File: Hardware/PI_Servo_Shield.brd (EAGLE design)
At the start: 65 x 30 mm, 89 parts, among them J1 RASPBERRYPI-40-PIN-GPIO, J19 QWIIC, J20 USB C, J21 Serial, U1 PCA9685, U2 PCA9306, U3 CH340C

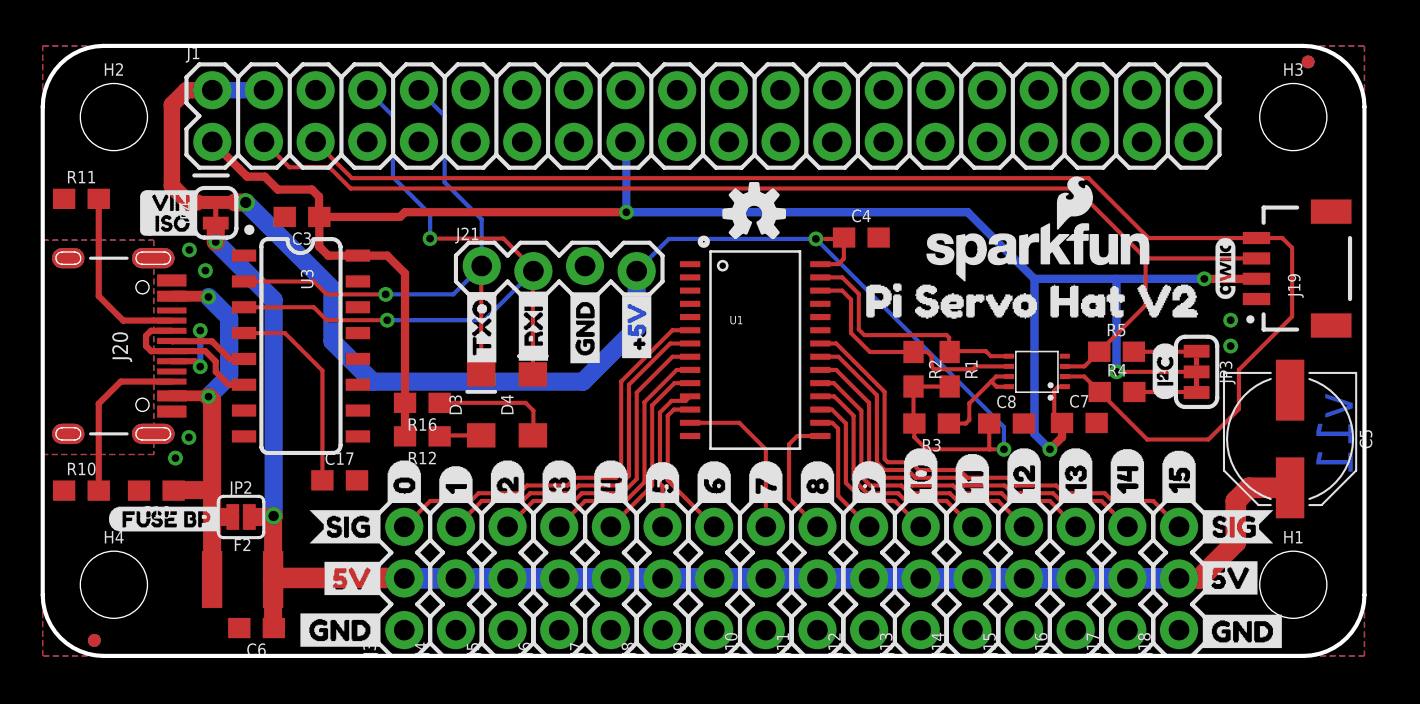
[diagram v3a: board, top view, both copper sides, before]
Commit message: post checklist changes - silk and testpoints
-silk outlines up to 8 mil on a few.
-testpoints
-RX/TX LED colors corrected
-some PROD_ID stuff fixed.
-text note in sch for i2c jumper
-voltage warning for > +5V RVR input damaging pi.
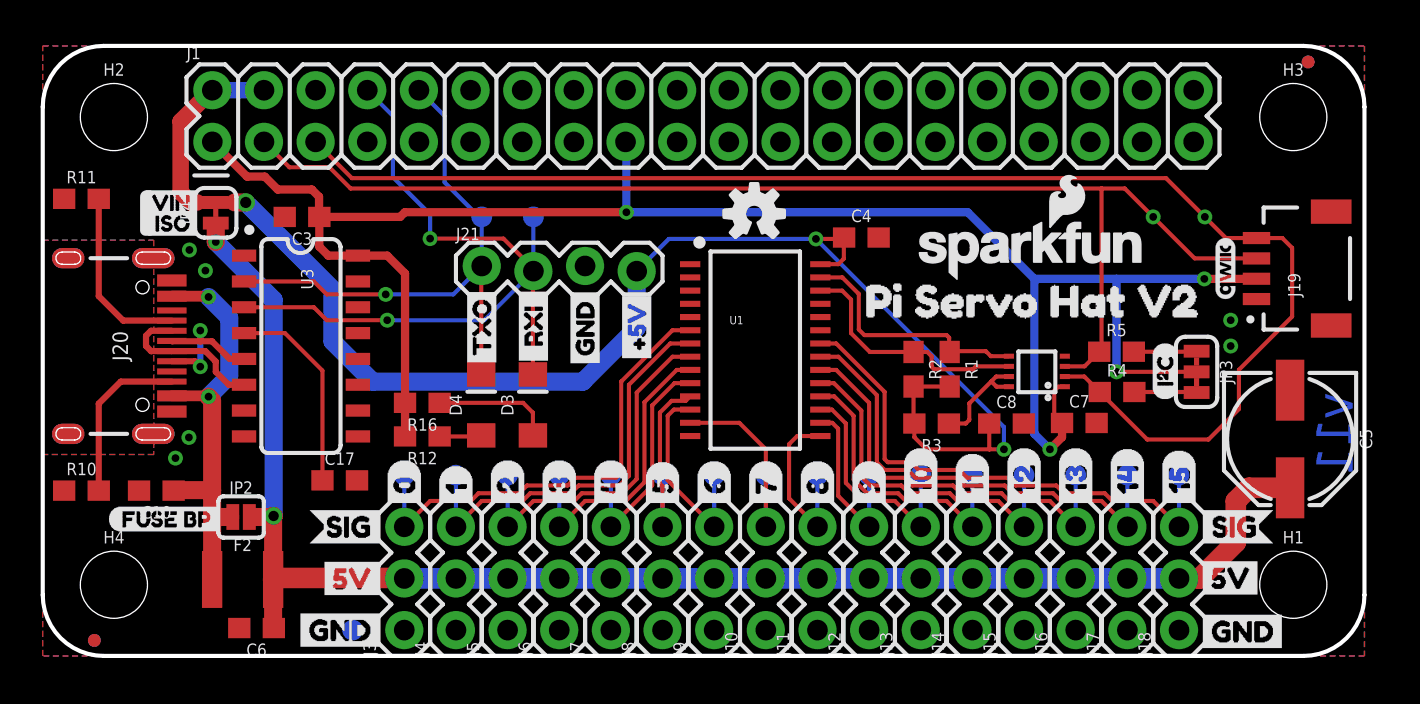
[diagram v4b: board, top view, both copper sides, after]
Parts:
- added TP0, TP1, TP10, TP11, TP12, TP13, TP14, TP15, TP16, TP17, TP2, TP20, TP21, TP3, TP4, TP5, TP6, TP7, TP8, TP9: (no value), SparkFun-Connectors:PAD.03X.04
- added TP18, TP19: (no value), SparkFun-Connectors:TP_15TH
- D4: device SparkFun-LED:LED-1206 -> SparkFun-LED:LED-1206-HIDDENSILK
- J20: device USB-C:USB-C-16P -> SparkFun-Connectors:USB-C-16P
- moved LOGO1 5.81 mm to (48.6, 20.0)
- moved D3 2.54 mm to (24.1, 12.3)
- moved D4 2.54 mm to (21.6, 12.3)
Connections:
- removed net N$12: D4.A, R16.1
- removed net N$13: D3.A, R12.1
- new net N$6: D3.A, R16.1
- new net N$7: D4.A, R12.1
- net CH0: now also TP0.P$1
- net CH1: now also TP1.P$1
- net CH10: now also TP10.P$1
- net CH11: now also TP11.P$1
- net CH12: now also TP12.P$1
- net CH13: now also TP13.P$1
- net CH14: now also TP14.P$1
- net CH15: now also TP15.P$1
- net CH2: now also TP2.P$1
- net CH3: now also TP3.P$1
- net CH4: now also TP4.P$1
- net CH5: now also TP5.P$1
- net CH6: now also TP6.P$1
- net CH7: now also TP7.P$1
- net CH8: now also TP8.P$1
- net CH9: now also TP9.P$1
- net GND: now also TP17.P$1
- net LV_SCL: now also TP18.P$1
- net LV_SDA: now also TP19.P$1
- net RXI: now also D3.C, TP20.P$1; no longer D4.C
- net TXO: now also D4.C, TP21.P$1; no longer D3.C
- net VIN: now also TP16.P$1
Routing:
- net N$12: track 6.00 -> 0.00 mm
- net N$6: track 0.00 -> 5.90 mm
- net RXI: track 35.1 -> 37.8 mm
- net VIN: track 75.5 -> 78.0 mm
- net CH14: track 20.5 -> 23.0 mm
- net CH12: track 14.8 -> 17.4 mm
- net CH0: track 20.7 -> 23.2 mm
- net CH9: track 6.45 -> 8.99 mm
- net CH8: track 6.35 -> 8.89 mm
- net CH5: track 7.49 -> 10.0 mm
- net CH7: track 8.07 -> 10.6 mm
- net CH6: track 7.64 -> 10.2 mm
- net CH4: track 9.13 -> 11.7 mm
- net CH3: track 11.9 -> 14.5 mm
- net CH11: track 12.0 -> 14.5 mm
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
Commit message: post double check stuff - moved from PCA9306 to transistors
-PCA level shifter is EOL, moved to transistor conversion.
-added VCC range note in SCH
-fixed a trace off of PCA PWM chip
-PROD_ID fixes on LEDs
-moved measure to show units
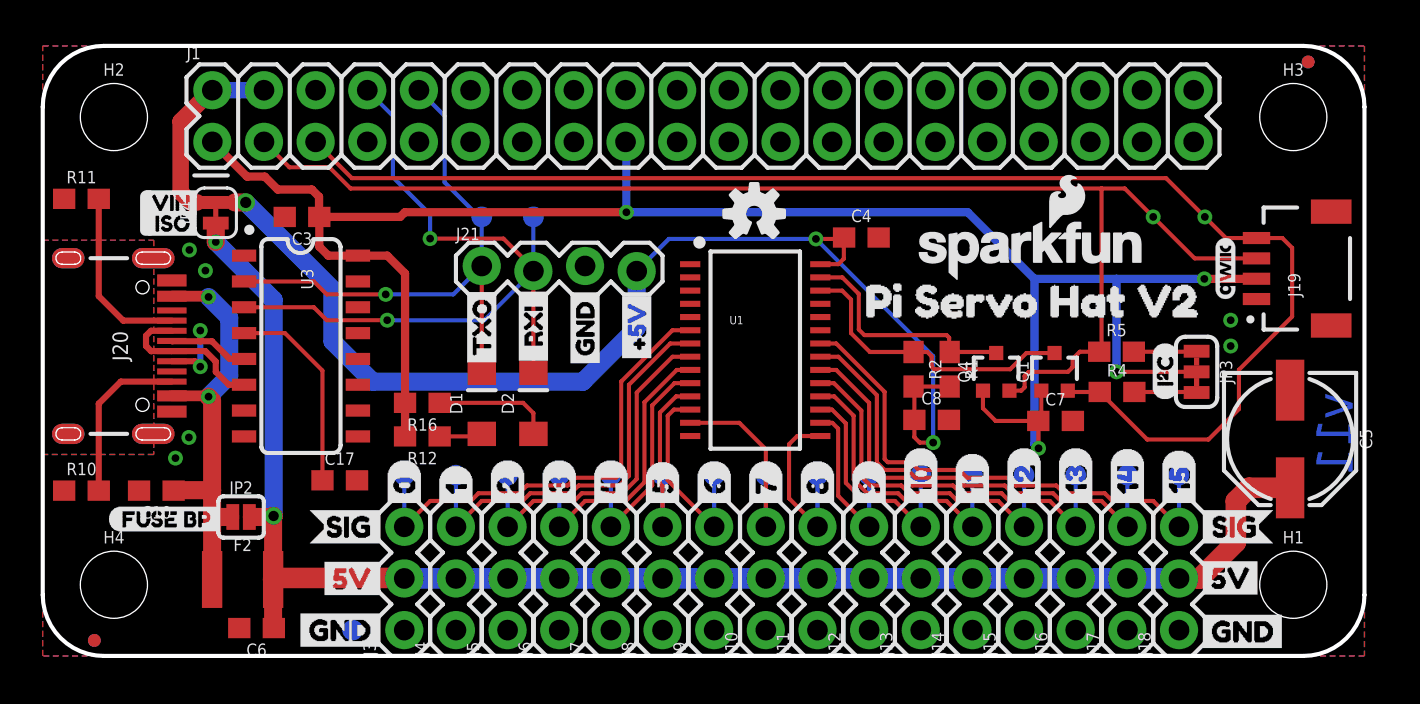
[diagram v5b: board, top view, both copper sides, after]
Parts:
- removed D3: Yellow, SparkFun-LED:LED-1206-HIDDENSILK
- removed D4: GREEN, SparkFun-LED:LED-1206-HIDDENSILK
- removed R3: 200k, SparkFun-Resistors:0603
- removed U2: PCA9306, SparkFun-IC-Comms:PSOP-8
- added D1: GREEN, SparkFun-LED:LED-1206-HIDDENSILK
- added D2: YELLOW, SparkFun-LED:LED-1206-HIDDENSILK
- added Q1, Q4: 2N7002PW, SparkFun-DiscreteSemi:SOT323
- moved C8 3.69 mm to (43.7, 11.6)
- moved C7 1.17 mm to (49.8, 11.6)
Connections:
- removed net N$1: R3.1, U2.7, U2.8
- net 3.3V: now also Q1.1, Q4.1; no longer U2.1
- net 5V: no longer R3.2
- net GND: no longer U2.4
- net LV_SCL: now also Q1.2; no longer U2.2
- net LV_SDA: now also Q4.2; no longer U2.3
- net N$3: now also Q1.3; no longer U2.6
- net N$4: now also Q4.3; no longer U2.5
- net N$6: now also D2.A; no longer D3.A
- net N$7: now also D1.A; no longer D4.A
- net RXI: now also D2.C; no longer D3.C
- net TXO: now also D1.C; no longer D4.C
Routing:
- net 5V: track 77.6 -> 71.0 mm
- net N$1: track 5.36 -> 0.00 mm
- net LV_SDA: track 61.2 -> 65.0 mm
- net 3.3V: track 93.7 -> 96.3 mm
- net N$3: track 12.2 -> 14.7 mm
- net N$4: track 12.3 -> 11.7 mm
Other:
- board text removed: "Dimensions given in mm"
- board text removed: "typ."

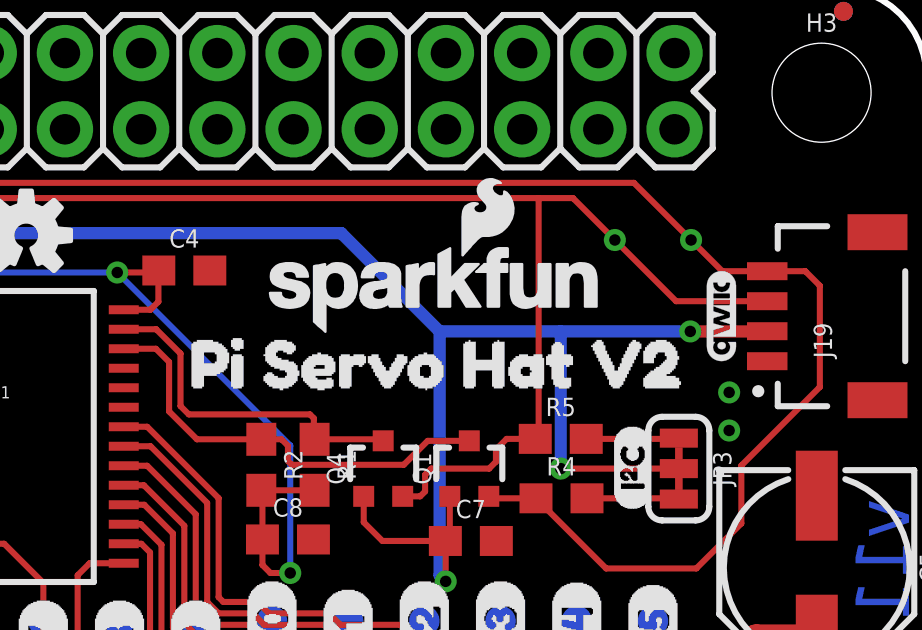
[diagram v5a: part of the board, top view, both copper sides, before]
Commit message: Bumped the QWIIC label to 5mm package
didn't print very cleanly at the 3mm size on the protos from jlcpcb, so bumped it up to 5mm package.
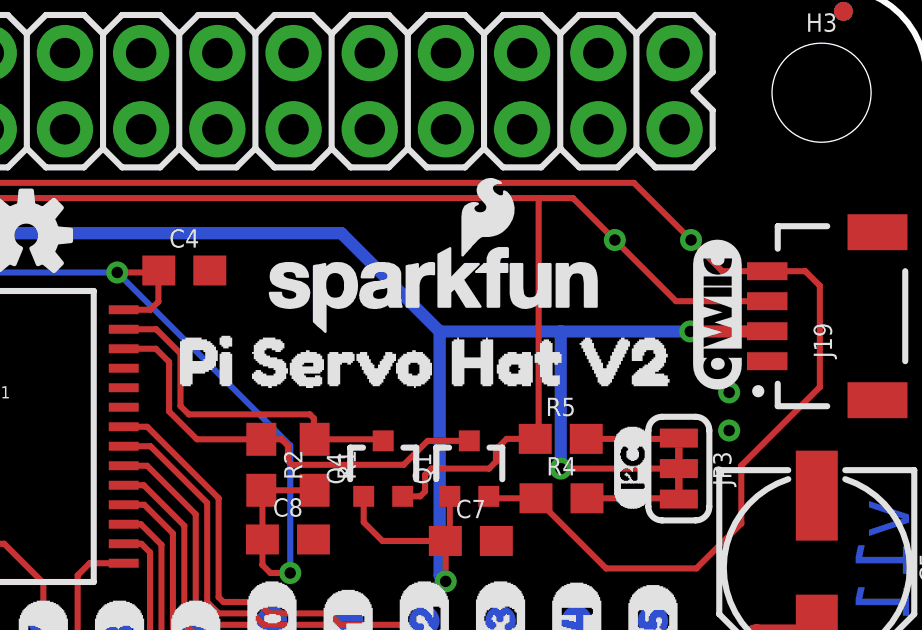
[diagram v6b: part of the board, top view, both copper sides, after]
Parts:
- U$1: value QWIIC_LOGO_3MM -> QWIIC_LOGO_5MM; device SparkFun-Aesthetics:QWIIC_3MM -> SparkFun-Aesthetics:QWIIC_5MM
- moved U$29 0.39 mm to (38.7, 17.5)
- moved U$1 0.15 mm to (58.0, 19.1)
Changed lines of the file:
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@@
 <layer number="27" name="tValues" color="7" fill="1" visible="no" active="yes"/>
 <layer number="28" name="bValues" color="7" fill="1" visible="no" active="yes"/>
-<layer number="29" name="tStop" color="7" fill="3" visible="no" active="yes"/>
+<layer number="29" name="tStop" color="7" fill="3" visible="yes" active="yes"/>
 <layer number="30" name="bStop" color="7" fill="6" visible="no" active="yes"/>
 <layer number="31" name="tCream" color="7" fill="4" visible="no" active="yes"/>
@@
 <attribute name="VALUE" x="20.32" y="17.018" size="0.6096" layer="27" font="vector" ratio="20"/>
 </element>
-<element name="U$1" library="SparkFun-Aesthetics" package="QWIIC_3MM" value="QWIIC_LOGO_3MM" x="58.166" y="19.05" smashed="yes" rot="R90"/>
+<element name="U$1" library="SparkFun-Aesthetics" package="QWIIC_5MM" value="QWIIC_LOGO_5MM" x="58.0136" y="19.0754" smashed="yes" rot="R90"/>
 <element name="C10" library="SparkFun-Capacitors" package="0603" value="0.1uF" x="5.588" y="8.128" smashed="yes" rot="R180">
 <attribute name="NAME" x="5.588" y="7.366" size="0.6096" layer="25" font="vector" ratio="20" rot="R180" align="bottom-center"/>
@@
 <attribute name="VALUE" x="9.652" y="21.7932" size="0.6096" layer="27" font="vector" ratio="20" rot="R90" align="top-center"/>
 </element>
-<element name="U$29" library="buzzard_labels (10)" package="PI_SERVO_HAT_V21" value="" x="39.116" y="17.4498" smashed="yes"/>
+<element name="U$29" library="buzzard_labels (10)" package="PI_SERVO_HAT_V21" value="" x="38.735" y="17.526" smashed="yes"/>
 <element name="TP0" library="SparkFun-Connectors" package="PAD.03X.04" value="" x="17.78" y="8.89" smashed="yes" rot="MR270"/>
 <element name="TP1" library="SparkFun-Connectors" package="PAD.03X.04" value="" x="20.32" y="8.89" smashed="yes" rot="MR270"/>

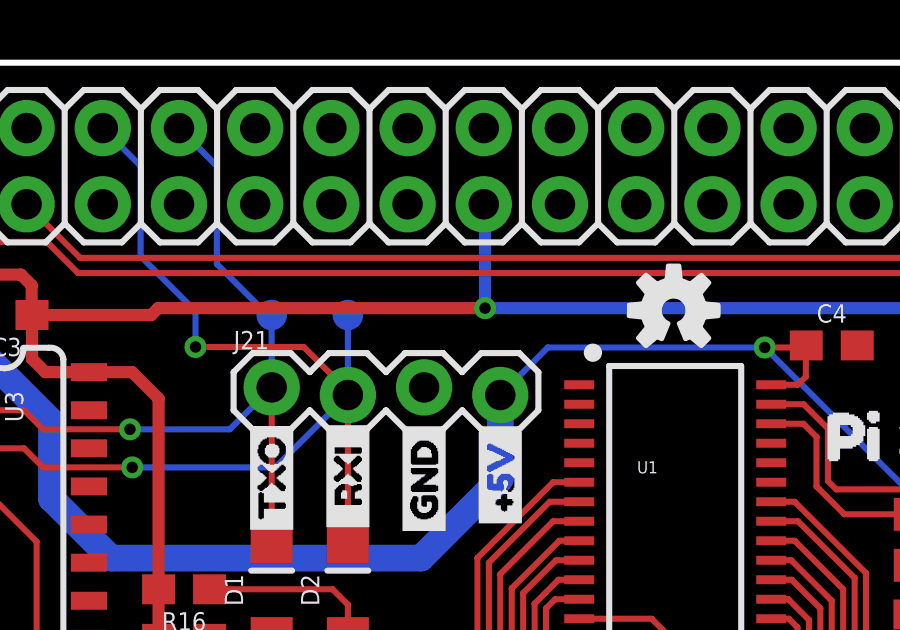
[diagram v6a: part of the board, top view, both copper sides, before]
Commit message: Added 3.3V test point - gonna need this for properly testing the CH340
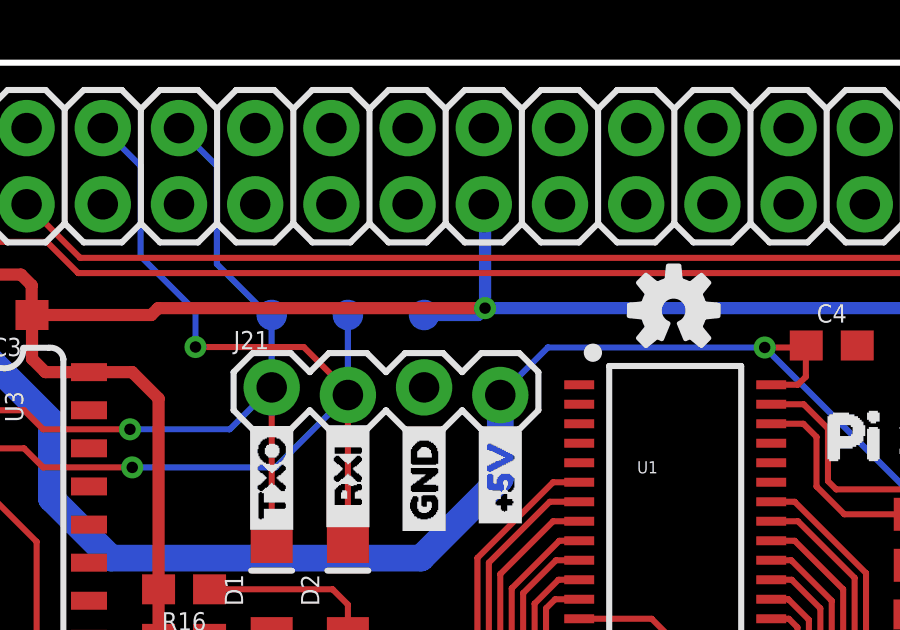
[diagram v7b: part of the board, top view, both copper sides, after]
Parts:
- added TP22: (no value), SparkFun-Connectors:PAD.03X.04
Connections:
- net 3.3V: now also TP22.P$1
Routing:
- net 3.3V: track 96.3 -> 98.4 mm
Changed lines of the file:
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@@
 <attribute name="VALUE" x="48.1584" y="13.97" size="0.6096" layer="27" font="vector" ratio="20" rot="R90" align="top-center"/>
 </element>
+<element name="TP22" library="SparkFun-Connectors" package="PAD.03X.04" value="" x="26.67" y="21.59" smashed="yes" rot="MR0"/>
 </elements>
 <signals>
@@
 <wire x1="46.863" y1="11.557" x2="48.9594" y2="11.557" width="0.2032" layer="1"/>
 <wire x1="46.2384" y1="12.1816" x2="46.863" y2="11.557" width="0.2032" layer="1"/>
+<contactref element="TP22" pad="P$1"/>
+<wire x1="28.4734" y1="21.59" x2="28.702" y2="21.8186" width="0.4064" layer="16"/>
+<wire x1="26.67" y1="21.59" x2="28.4734" y2="21.59" width="0.4064" layer="16"/>
 </signal>
 <signal name="N$6">
